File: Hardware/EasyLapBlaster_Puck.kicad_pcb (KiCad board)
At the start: 2 copper layers, 55.3 x 121.9 mm, 34 parts, among them IC1 PIC10F322, P1 CONN_01X02, P2 CONN_01X06, Q1 AO3401A, Q2 AO3400A, SW1 SPST, U1 HS0038B, U2 DW-01, U3 FS8205

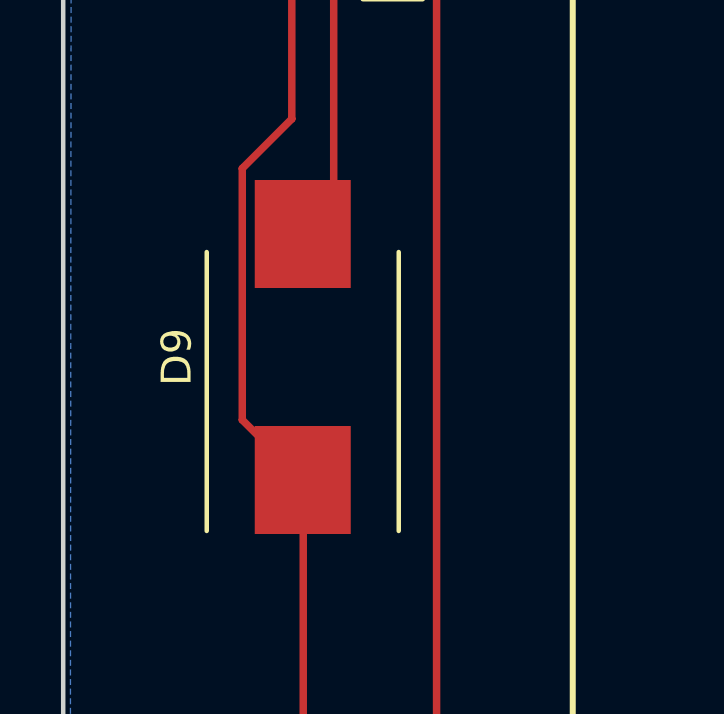
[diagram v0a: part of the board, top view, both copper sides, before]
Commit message: added LED footprint, rearranged led/resistor order for better heatsinking (VCC can be poured on the top layer)
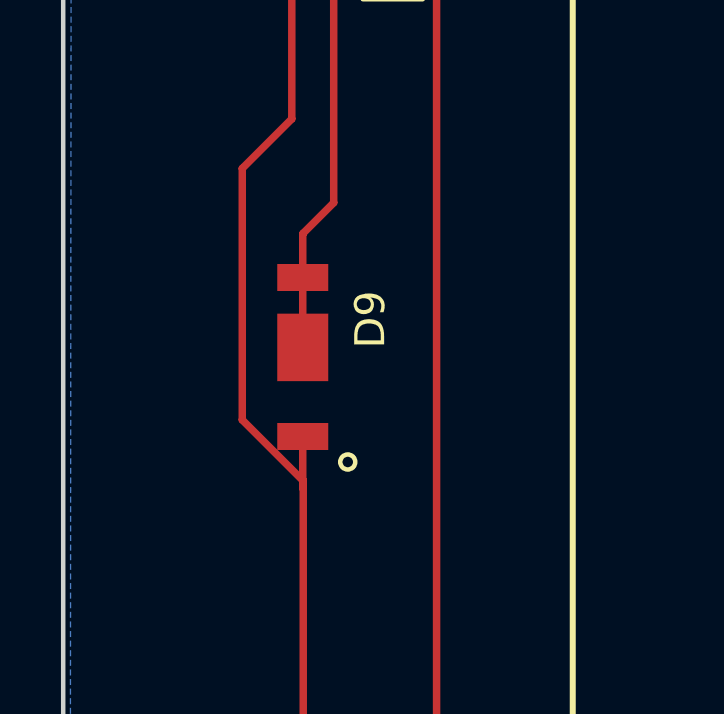
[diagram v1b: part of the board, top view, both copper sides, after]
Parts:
- D9: footprint Diodes_SMD:DO-214AB_Handsoldering -> bengineeringlabs:5730LED
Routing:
- net Net-(D9-Pad2): track 9.38 -> 13.2 mm
- net Net-(D1-Pad1): track 269.3 -> 271.2 mm
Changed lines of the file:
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@@
 (kicad_pcb (version 4) (host pcbnew 4.0.2-stable)
   (general
-    (links 61)
+    (links 62)
     (no_connects 2)
-    (area 119.908328 39.929999 175.335001 165.19648)
+    (area 119.908328 39.929999 175.335001 162.000001)
     (thickness 1.6)
     (drawings 12)
-    (tracks 403)
+    (tracks 408)
     (zones 0)
     (modules 34)
@@
   )
   (module Diodes_SMD:DO-214AB_Handsoldering (layer F.Cu)
-    (at 128 75.5 90)
-    (descr "Jedec DO-214AB diode package. Designed according to Fairchild SS32 datasheet.")
-    (tags "DO-214AB diode Handsoldering")
-    (attr smd)
-    (fp_text reference D9 (at 0 -4.2 90) (layer F.SilkS)
-      (effects (font (size 1 1) (thickness 0.15)))
-    )
-    (fp_text value LED (at 0 4.6 90) (layer F.Fab)
-      (effects (font (size 1 1) (thickness 0.15)))
-    )
-    (fp_line (start -6.15 -3.45) (end 6.15 -3.45) (layer F.CrtYd) (width 0.05))
-    (fp_line (start 6.15 -3.45) (end 6.15 3.45) (layer F.CrtYd) (width 0.05))
-    (fp_line (start 6.15 3.45) (end -6.15 3.45) (layer F.CrtYd) (width 0.05))
-    (fp_line (start -6.15 3.45) (end -6.15 -3.45) (layer F.CrtYd) (width 0.05))
-    (fp_line (start 3.5 3.2) (end -5.8 3.2) (layer F.SilkS) (width 0.15))
-    (fp_line (start -5.8 -3.2) (end 3.5 -3.2) (layer F.SilkS) (width 0.15))
-    (pad 2 smd rect (at 4.1 0 90) (size 3.6 3.2) (layers F.Cu F.Paste F.Mask)
-      (net 25 "Net-(D9-Pad2)"))
-    (pad 1 smd rect (at -4.1 0 90) (size 3.6 3.2) (layers F.Cu F.Paste F.Mask)
-      (net 8 "Net-(D1-Pad1)"))
-    (model Diodes_SMD.3dshapes/DO-214AB_Handsoldering.wrl
-      (at (xyz 0 0 0))
-      (scale (xyz 0.39 0.39 0.39))
-      (rotate (xyz 0 0 180))
-    )
-  )
-  (module Diodes_SMD:DO-214AB_Handsoldering (layer F.Cu)
     (at 128.27 50.165 90)
     (descr "Jedec DO-214AB diode package. Designed according to Fairchild SS32 datasheet.")
@@
       (rotate (xyz 0 0 0))
     )
+  )
+  (module bengineeringlabs:5730LED (layer F.Cu)
+    (at 128 75.5 90)
+    (fp_text reference D9 (at 1.25 2.25 90) (layer F.SilkS)
+      (effects (font (size 1 1) (thickness 0.15)))
+    )
+    (fp_text value LED (at 0.25 -2 90) (layer F.Fab)
+      (effects (font (size 1 1) (thickness 0.15)))
+    )
+    (fp_circle (center -3.5 1.5) (end -3.5 1.75) (layer F.SilkS) (width 0.15))
+    (pad 2 smd rect (at 0.32 0 90) (size 2.25 1.7) (layers F.Cu F.Paste F.Mask)
+      (net 25 "Net-(D9-Pad2)"))
+    (pad 2 smd rect (at 2.65 0 90) (size 0.9 1.7) (layers F.Cu F.Paste F.Mask)
+      (net 25 "Net-(D9-Pad2)"))
+    (pad 1 smd rect (at -2.65 0 90) (size 0.9 1.7) (layers F.Cu F.Paste F.Mask)
+      (net 8 "Net-(D1-Pad1)"))
   )
   (gr_line (start 120.015 156.21) (end 120.015 46.99) (angle 90) (layer Edge.Cuts) (width 0.15))
@@
   (segment (start 153.035 154.432) (end 154.94 152.527) (width 0.25) (layer F.Cu) (net 7) (status 80020))
   (segment (start 154.94 152.527) (end 155 152.5) (width 0.25) (layer F.Cu) (net 7) (status 80030))
+  (segment (start 128 78.15) (end 128 79.87) (width 0.25) (layer F.Cu) (net 8) (status 400000))
+  (segment (start 128.016 79.854) (end 128.016 79.629) (width 0.25) (layer F.Cu) (net 8))
+  (segment (start 128 79.87) (end 128.016 79.854) (width 0.25) (layer F.Cu) (net 8))
   (segment (start 141 152.50178) (end 140.97 152.527) (width 0.25) (layer F.Cu) (net 8) (status 80030))
   (segment (start 140.97 152.527) (end 140.589 152.146) (width 0.25) (layer F.Cu) (net 8) (status 80010))
@@
   (segment (start 128.016 91.059) (end 128.016 100.838) (width 0.25) (layer F.Cu) (net 24) (status 80030))
   (segment (start 128.016 100.838) (end 128 100.9) (width 0.25) (layer F.Cu) (net 24) (status 80030))
+  (segment (start 128 75.18) (end 128 72.85) (width 0.25) (layer F.Cu) (net 25) (status C00000))
+  (segment (start 128 72.85) (end 128 71.4) (width 0.25) (layer F.Cu) (net 25) (status 400000))
+  (segment (start 129.032 70.358) (end 129.032 62.484) (width 0.25) (layer F.Cu) (net 25) (status 80030))
+  (segment (start 128.016 71.374) (end 129.032 70.358) (width 0.25) (layer F.Cu) (net 25) (status 80030))
   (segment (start 128 71.4) (end 128.016 71.374) (width 0.25) (layer F.Cu) (net 25) (status 80030))
-  (segment (start 128.016 71.374) (end 129.032 70.358) (width 0.25) (layer F.Cu) (net 25) (status 80030))
-  (segment (start 129.032 70.358) (end 129.032 62.484) (width 0.25) (layer F.Cu) (net 25) (status 80030))
   (segment (start 129.032 62.484) (end 129 62.5) (width 0.25) (layer F.Cu) (net 25) (status 80030))
   (segment (start 128.27 46.065) (end 128.27 46.101) (width 0.25) (layer F.Cu) (net 26) (status 80030))

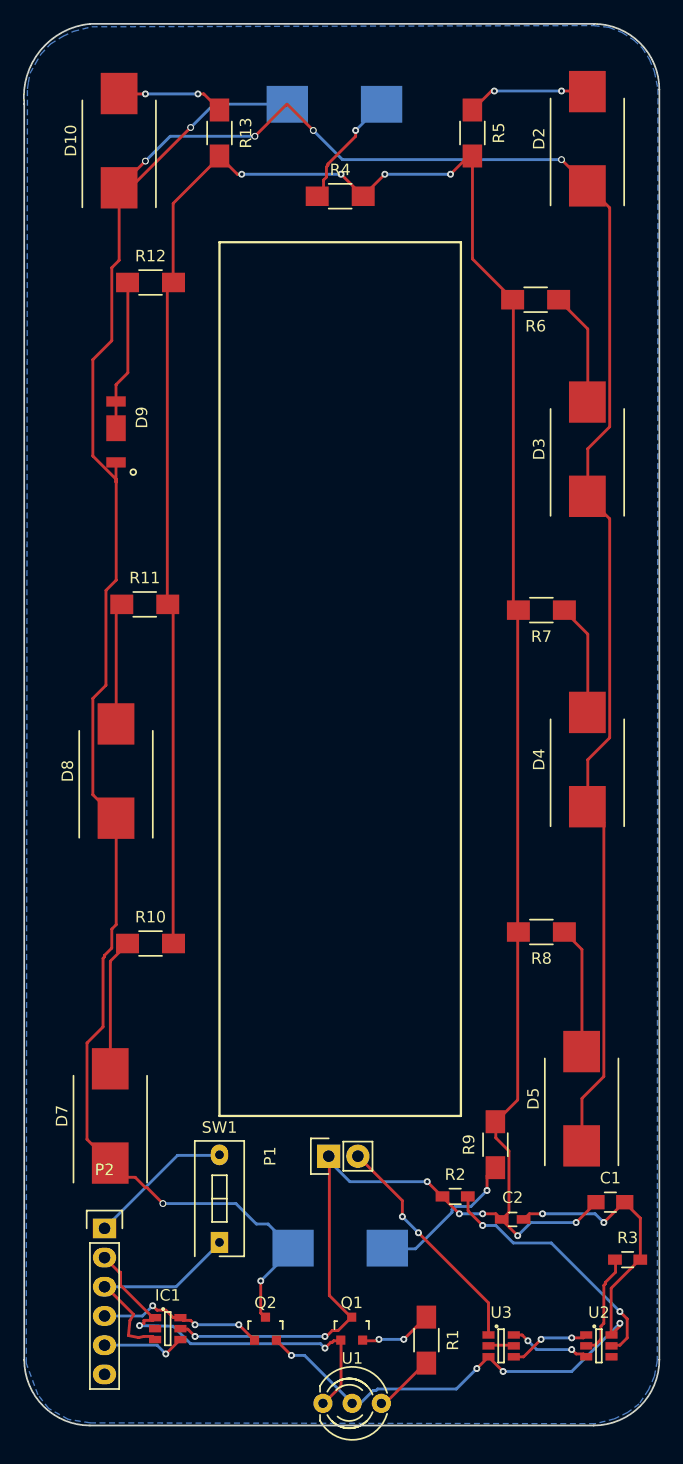
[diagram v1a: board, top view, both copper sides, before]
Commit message: netlist updated on board file, layout is still a mess
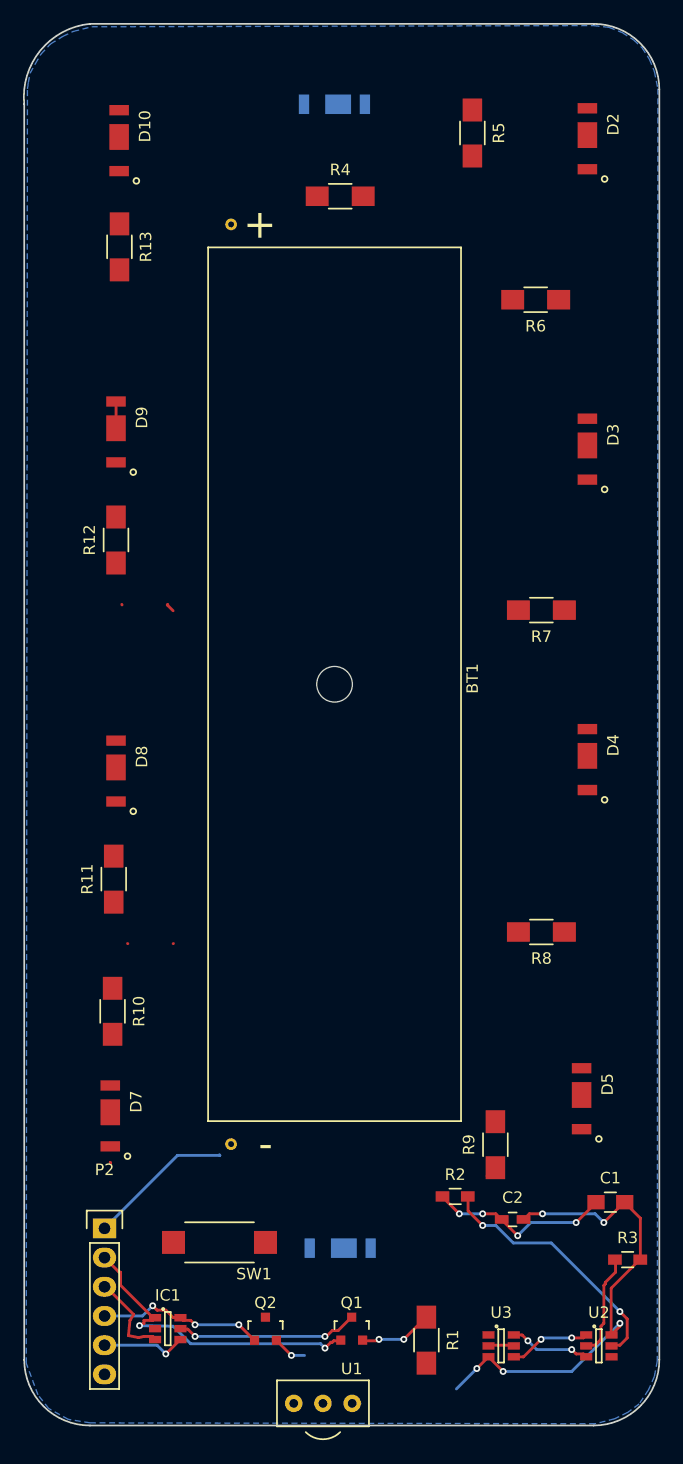
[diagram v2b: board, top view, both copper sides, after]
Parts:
- removed P1: CONN_01X02, Pin_Headers:Pin_Header_Straight_1x02
- added BT1: Battery, bengineeringlabs:18650BatHolder, F.Cu at (147.0, 97.5)
- D1, D10, D2, D3, D4, D5, D6, D7, D8: footprint Diodes_SMD:DO-214AB_Handsoldering -> bengineeringlabs:5730LED
- SW1: footprint Buttons_Switches_ThroughHole:SW_DIP_x1_Slide -> bengineeringlabs:SMD_SW_2PAD
- U1: footprint LEDs:LED-5MM-3 -> bengineeringlabs:HS0038B
- moved R11 24.1 mm to (127.8, 114.4), turned to 90 degrees
- moved R12 22.6 mm to (128.0, 84.9), turned to 90 degrees
- moved R13 13.2 mm to (128.3, 59.4)
- moved R10 6.76 mm to (127.7, 125.9), turned to 270 degrees
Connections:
- D1 pad 2: Net-(D1-Pad2) -> /Vbat
- D10 pad 1: Net-(D1-Pad1) -> Net-(D10-Pad1)
- D10 pad 2: Net-(D10-Pad2) -> /Vbat
- D2 pad 1: Net-(D1-Pad1) -> Net-(D2-Pad1)
- D2 pad 2: Net-(D2-Pad2) -> /Vbat
- D3 pad 1: Net-(D1-Pad1) -> Net-(D3-Pad1)
- D3 pad 2: Net-(D3-Pad2) -> /Vbat
- D4 pad 1: Net-(D1-Pad1) -> Net-(D4-Pad1)
- D4 pad 2: Net-(D4-Pad2) -> /Vbat
- D5 pad 1: Net-(D1-Pad1) -> Net-(D5-Pad1)
- D5 pad 2: Net-(D5-Pad2) -> /Vbat
- D6 pad 1: Net-(D1-Pad1) -> Net-(D6-Pad1)
- D6 pad 2: Net-(D6-Pad2) -> /Vbat
- D7 pad 1: Net-(D1-Pad1) -> Net-(D7-Pad1)
- D7 pad 2: Net-(D7-Pad2) -> /Vbat
- D8 pad 1: Net-(D1-Pad1) -> Net-(D8-Pad1)
- D8 pad 2: Net-(D8-Pad2) -> /Vbat
- D9 pad 1: Net-(D1-Pad1) -> Net-(D9-Pad1)
- D9 pad 2: Net-(D9-Pad2) -> /Vbat
- Q2 pad 3: Net-(D1-Pad1) -> Net-(Q2-Pad3)
- R10 pad 1: Net-(D7-Pad2) -> Net-(Q2-Pad3)
- R10 pad 2: /Vbat -> Net-(D7-Pad1)
- R11 pad 1: Net-(D8-Pad2) -> Net-(Q2-Pad3)
- R11 pad 2: /Vbat -> Net-(D8-Pad1)
- R12 pad 1: Net-(D9-Pad2) -> Net-(Q2-Pad3)
- R12 pad 2: /Vbat -> Net-(D9-Pad1)
- R13 pad 1: Net-(D10-Pad2) -> Net-(Q2-Pad3)
- R13 pad 2: /Vbat -> Net-(D10-Pad1)
- R4 pad 1: Net-(D1-Pad2) -> Net-(Q2-Pad3)
- R4 pad 2: /Vbat -> Net-(D1-Pad1)
- R5 pad 1: Net-(D2-Pad2) -> Net-(Q2-Pad3)
- R5 pad 2: /Vbat -> Net-(D2-Pad1)
- R6 pad 1: Net-(D3-Pad2) -> Net-(Q2-Pad3)
- R6 pad 2: /Vbat -> Net-(D3-Pad1)
- R7 pad 1: Net-(D4-Pad2) -> Net-(Q2-Pad3)
- R7 pad 2: /Vbat -> Net-(D4-Pad1)
- R8 pad 1: Net-(D5-Pad2) -> Net-(Q2-Pad3)
- R8 pad 2: /Vbat -> Net-(D5-Pad1)
- R9 pad 1: Net-(D6-Pad2) -> Net-(Q2-Pad3)
- R9 pad 2: /Vbat -> Net-(D6-Pad1)
- U2 pad 4: Net-(U2-Pad4) -> (no net)
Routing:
- net Net-(D1-Pad1): track 271.2 -> 0.02 mm, vias 7 -> 0
- net /Vbat: track 250.1 -> 34.6 mm, vias 11 -> 6
- net /V-: track 20.3 -> 0.00 mm, vias 2 -> 0
- net /GND: track 73.6 -> 58.1 mm
- net Net-(D6-Pad2): track 13.5 -> 0.00 mm, vias 1 -> 0
- net Net-(D9-Pad2): track 13.2 -> 0.00 mm
- net /RA1: track 20.0 -> 8.38 mm
- net Net-(D7-Pad2): track 11.6 -> 0.00 mm
- net Net-(D5-Pad2): track 11.1 -> 0.00 mm
- net Net-(D2-Pad2): track 10.8 -> 0.00 mm, vias 2 -> 0
- net Net-(D8-Pad2): track 10.6 -> 0.00 mm
- net Net-(D1-Pad2): track 10.4 -> 0.00 mm, vias 1 -> 0
- net Net-(D3-Pad2): track 9.99 -> 0.00 mm
- net Net-(D4-Pad2): track 9.85 -> 0.00 mm
- net Net-(D10-Pad2): track 9.41 -> 0.00 mm, vias 2 -> 0
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
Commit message: Keith's Changes: Slimmed down board, organized components added .gitattributes & .gitignore
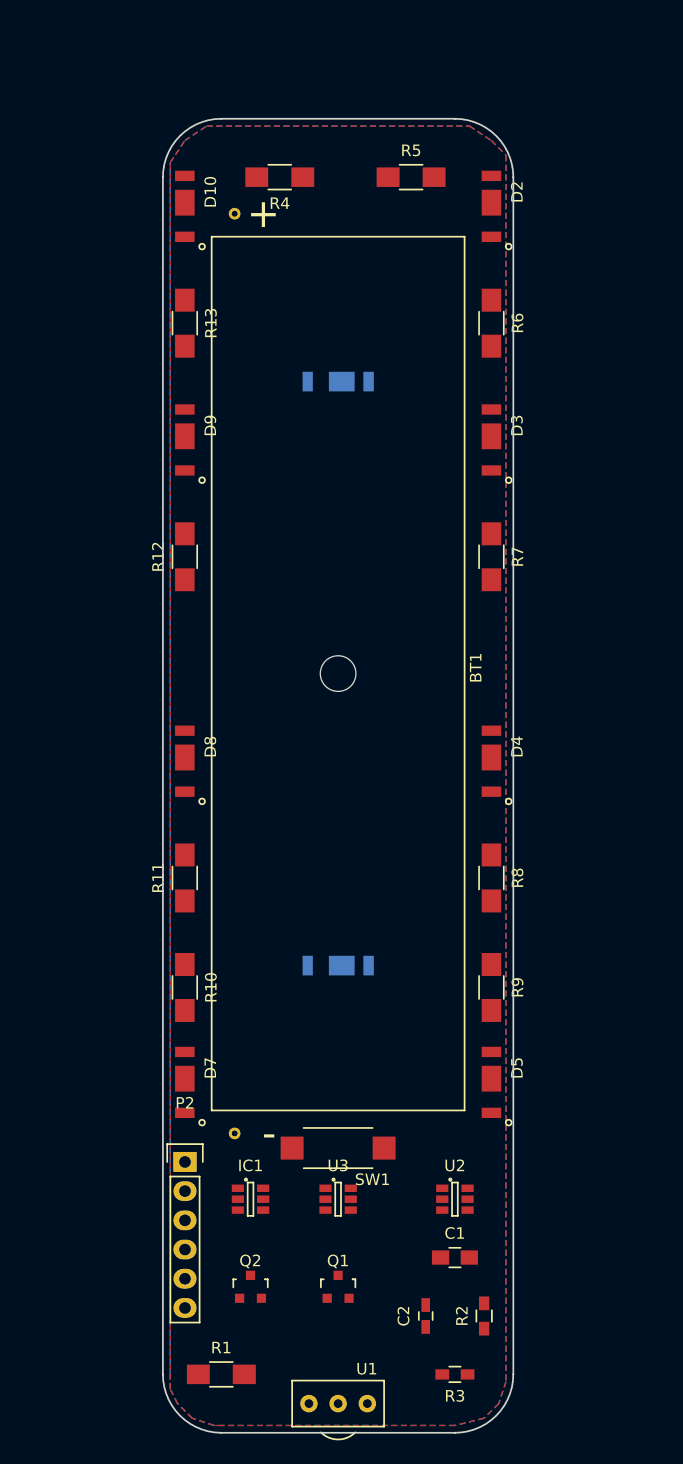
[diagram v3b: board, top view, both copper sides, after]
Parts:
- R3: value 1000 -> 1K
- moved D6 24.6 mm to (147.3, 121.9)
- moved D1 24.1 mm to (147.3, 71.1)
- moved U3 19.1 mm to (147.3, 142.2)
- moved R1 18.1 mm to (137.2, 157.5), turned to 0 degrees
- moved R3 18.0 mm to (157.5, 157.5), turned to 180 degrees
- moved U2 17.9 mm to (157.5, 142.2)
- moved C1 14.4 mm to (157.5, 147.3)
- moved R9 13.7 mm to (160.7, 123.8), turned to 270 degrees
- moved IC1 13.4 mm to (139.7, 142.2)
- moved SW1 13.2 mm to (147.3, 137.8)
- moved C2 11.3 mm to (154.9, 152.4), turned to 90 degrees
- moved R2 10.7 mm to (160.0, 152.4), turned to 90 degrees
- moved D2 10.2 mm to (160.7, 55.9)
- moved P2 9.08 mm to (134.0, 139.0)
- moved R13 8.74 mm to (134.0, 66.0)
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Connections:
- U2 pad 4: (no net) -> Net-(U2-Pad4)
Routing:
- net /GND: track 58.1 -> 0.00 mm, vias 6 -> 0
- net /Vbat: track 34.6 -> 0.00 mm, vias 6 -> 0
- net /RA0: track 28.7 -> 0.00 mm, vias 2 -> 0
- net Net-(R2-Pad2): track 22.4 -> 0.00 mm, vias 2 -> 0
- net /RA2: track 15.2 -> 0.00 mm, vias 3 -> 0
- net Net-(R3-Pad1): track 9.13 -> 0.00 mm
- net /RA1: track 8.38 -> 0.00 mm
- net /RA3: track 7.46 -> 0.00 mm, vias 1 -> 0
- net /G2: track 7.19 -> 0.00 mm, vias 2 -> 0
- net /G1: track 7.19 -> 0.00 mm, vias 2 -> 0
- net Net-(Q1-Pad2): track 6.43 -> 0.00 mm, vias 2 -> 0
- net /D12: track 2.29 -> 0.00 mm
- net Net-(Q2-Pad3): track 2.02 -> 0.00 mm
- net (no net): track 1.02 -> 0.00 mm
- net Net-(R1-Pad2): track 0.76 -> 0.00 mm
- added copper zone on F.Cu, net /Vbat
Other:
- board size 55.3 x 121.9 mm -> 30.5 x 114.3 mm

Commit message: Added power traces.
Need to widen board and Vcc/Gnd fill areas.
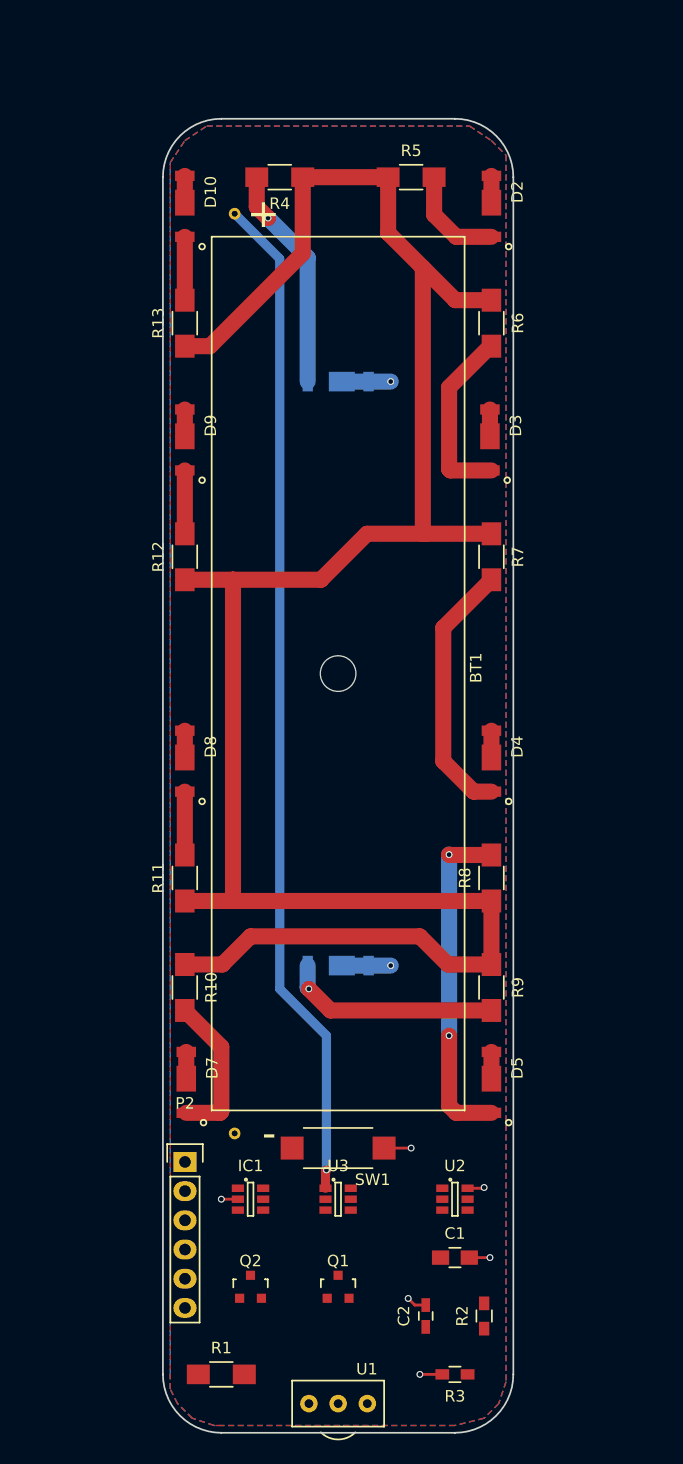
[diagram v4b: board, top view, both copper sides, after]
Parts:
- moved D3 0.13 mm to (160.5, 76.2)
- moved D7 0.13 mm to (134.1, 132.1)
- turned R13 to 90 degrees
- turned R8 to 90 degrees
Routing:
- net Net-(Q2-Pad3): track 0.00 -> 184.6 mm
- net /V-: track 0.00 -> 88.1 mm, vias 0 -> 1
- net Net-(D5-Pad1): track 0.00 -> 29.5 mm, vias 0 -> 2
- net /Vbat: track 0.00 -> 27.1 mm, vias 0 -> 2
- net Net-(D4-Pad1): track 0.00 -> 22.8 mm
- net Net-(D1-Pad1): track 0.00 -> 19.6 mm, vias 0 -> 1
- net Net-(D6-Pad1): track 0.00 -> 18.7 mm, vias 0 -> 1
- net Net-(D3-Pad1): track 0.00 -> 16.0 mm
- net Net-(D7-Pad1): track 0.00 -> 13.2 mm
- net /GND: track 0.00 -> 10.8 mm, vias 0 -> 6
- net Net-(D2-Pad1): track 0.00 -> 9.05 mm
- net Net-(D9-Pad1): track 0.00 -> 5.51 mm
- net Net-(D10-Pad1): track 0.00 -> 5.51 mm
- net Net-(D8-Pad1): track 0.00 -> 5.51 mm
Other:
- net class Battery - added: clearance 0.1, trace_width 0.8, via_dia 0.6, via_drill 0.4
- net class Default: clearance 0.2 -> 0; trace_width 0.25 -> 1.4
- rule trace_clearance: 0.2 -> 0
